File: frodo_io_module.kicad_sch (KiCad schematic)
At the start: 123 parts, among them J1 Molex MicroFit 2x3, J1 SWD, J2 Molex MicroFit 2x3, J4 JST-GH 4Pin, Q17 NMOS, Q18 NMOS, SW1 SW_DIP_x06, U1 AZ1117H-ADJ, U1 STM32F072RBT6, U3 AZ1117-3.3, U4 W25Q128JVP, U5 MCP2562-E-SN, U6 L7805, U7 L7805, U8 MCP4017-xxxxLT, U9 LM3488MM, Y1 8MHz 12pF

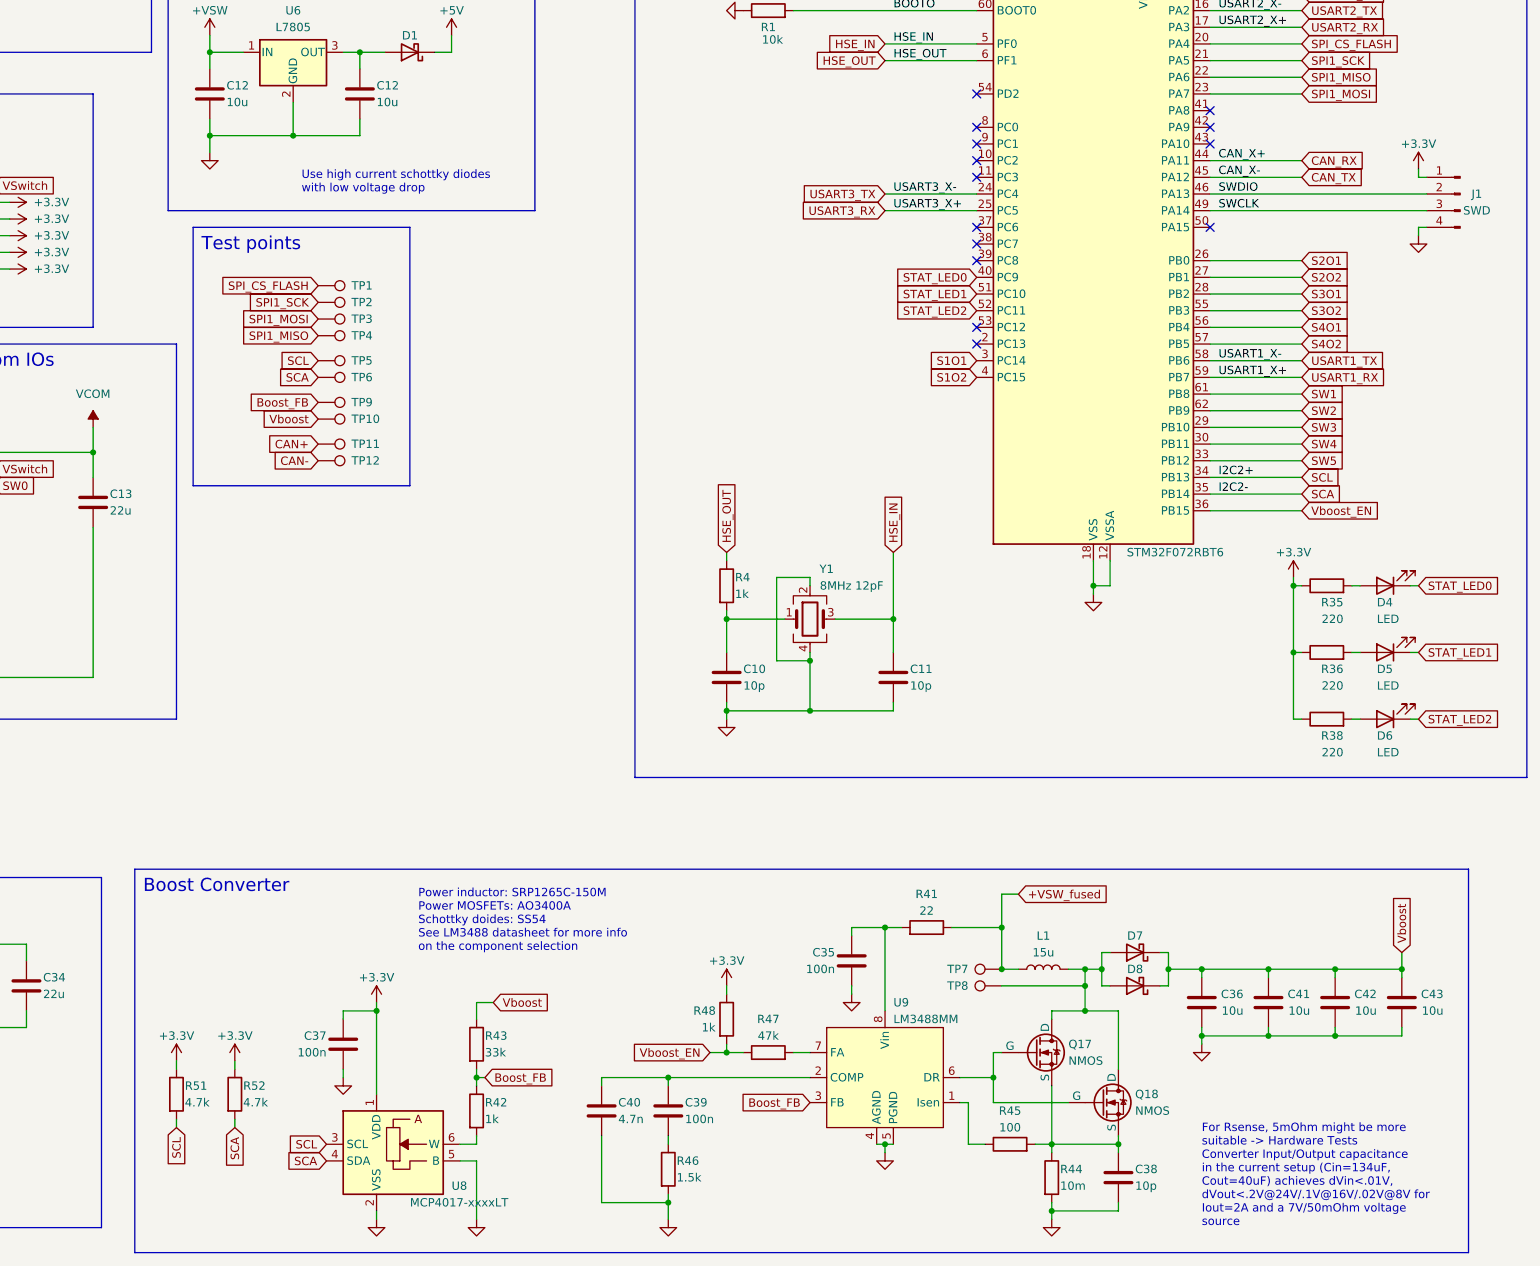
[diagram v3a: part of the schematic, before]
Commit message: Add voltage sensing, Correct resistor value
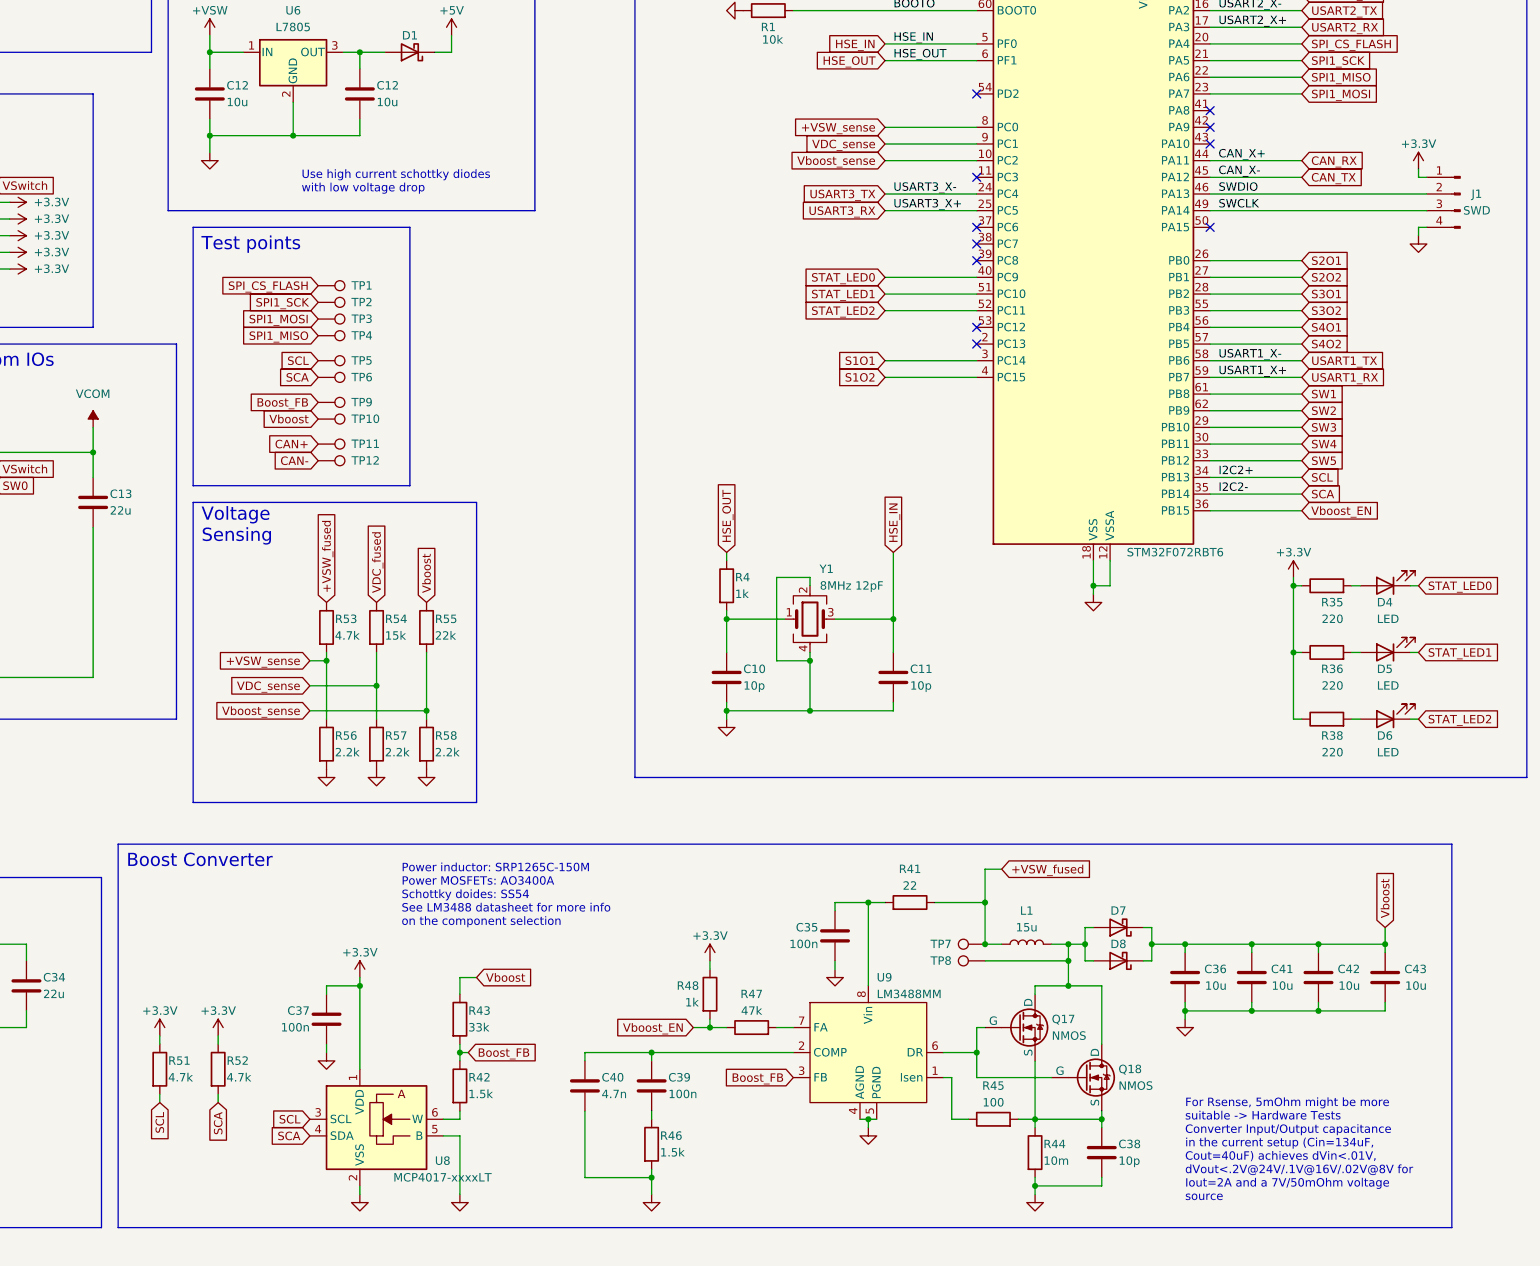
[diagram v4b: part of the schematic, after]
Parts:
- added R53: 4.7k, symbol Device:R
- added R54: 15k, symbol Device:R
- added R55: 22k, symbol Device:R
- added R56, R57, R58: 2.2k, symbol Device:R
- R42: value 1k -> 1.5k
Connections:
- net +VSW_fused: now also R53.1
- net GND: now also R56.2, R57.2, R58.2
- net VDC_fused: now also R54.1
- net Vboost: now also R55.1
- net Vboost_sense: now reaches U1.10 (PC2)
- net Vboost_sense: now also R55.2, R58.1
- net +VSW_sense: now reaches U1.8 (PC0)
- net +VSW_sense: now also R53.2, R56.1
- net VDC_sense: now reaches U1.9 (PC1)
- net VDC_sense: now also R54.2, R57.1
- no-connect marks 16 -> 13
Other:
- note added: "Voltage Sensing"
- moved on the sheet: C35, C36, C37, C38, C39, C40, C41, C42, C43, D7, D8, L1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

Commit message: footprints assigned
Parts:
- C1, C10, C11, C2, C3, C35, C37, C38, C39, C4, C9: footprint (none) -> Capacitor_SMD:C_0603_1608Metric_Pad1.08x0.95mm_HandSolder
- C12, C13, C25, C26, C27, C28, C30, C31, C32, C33, C34, C36, C41, C42, C43, C5: footprint (none) -> Capacitor_SMD:C_1206_3216Metric_Pad1.33x1.80mm_HandSolder
- C23, C24, C29, C6, C7, C8: footprint (none) -> Capacitor_SMD:C_0805_2012Metric_Pad1.18x1.45mm_HandSolder
- C43: footprint Capacitor_SMD:C_0402_1005Metric_Pad0.74x0.62mm_HandSolder -> Capacitor_SMD:C_0603_1608Metric_Pad1.08x0.95mm_HandSolder
- D3, D4, D5, D6: footprint (none) -> LED_SMD:LED_0603_1608Metric
- FB1: footprint (none) -> Ferrite_THT:LairdTech_28C0236-0JW-10
- J1, J2: footprint (none) -> Connector_Molex:Molex_Micro-Fit_3.0_43045-0600_2x03_P3.00mm_Horizontal
- J4: footprint (none) -> Connector_JST:JST_GH_SM04B-GHS-TB_1x04-1MP_P1.25mm_Horizontal
- Q17, Q18: footprint (none) -> Package_TO_SOT_SMD:SOT-23-3
- R1, R10, R4, R48, R5, R6, R7, R8, R9: footprint (none) -> Resistor_SMD:R_0603_1608Metric_Pad0.98x0.95mm_HandSolder
- R35, R36, R37, R38, R39, R40, R45: footprint (none) -> Resistor_SMD:R_0603_1608Metric
- U3: footprint (none) -> Package_TO_SOT_SMD:SOT-223-3_TabPin2
- U6, U7: footprint (none) -> Package_TO_SOT_SMD:TO-252-2
- Y1: footprint (none) -> Crystal:Crystal_SMD_5032-4Pin_5.0x3.2mm

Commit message: more footprints assigned
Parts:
- C40: footprint (none) -> Capacitor_SMD:C_1210_3225Metric_Pad1.33x2.70mm_HandSolder
- D1, D2, D7, D8: footprint (none) -> Diode_SMD:D_SOD-323_HandSoldering
- F1, F2: footprint (none) -> Fuse:Fuse_1206_3216Metric_Pad1.42x1.75mm_HandSolder
- J1, R1, R41, R42, R43, R44, R46, R49, R50, R51, R52, R53, R54, R55, R56, R57, R58: footprint (none) -> Resistor_SMD:R_0805_2012Metric_Pad1.20x1.40mm_HandSolder
- Q18: footprint Package_TO_SOT_SMD:SOT-23-3 -> Resistor_SMD:R_0805_2012Metric_Pad1.20x1.40mm_HandSolder
- R3, R47: footprint (none) -> Resistor_SMD:R_1206_3216Metric_Pad1.30x1.75mm_HandSolder
- R35, R36, R38, R39, R40, R45: footprint Resistor_SMD:R_0603_1608Metric -> Resistor_SMD:R_0603_1608Metric_Pad0.98x0.95mm_HandSolder
- R37: footprint Resistor_SMD:R_0603_1608Metric -> Resistor_SMD:R_0805_2012Metric_Pad1.20x1.40mm_HandSolder
- U9: footprint (none) -> Package_SO:TSSOP-8_4.4x3mm_P0.65mm
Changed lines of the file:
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@@
       (effects (font (size 1.27 1.27)) (justify left))
     )
-    (property "Footprint" "" (at 93.472 82.55 90)
+    (property "Footprint" "Resistor_SMD:R_0805_2012Metric_Pad1.20x1.40mm_HandSolder" (at 93.472 82.55 90)
       (effects (font (size 1.27 1.27)) hide)
     )
@@
       (effects (font (size 1.27 1.27)) (justify left))
     )
-    (property "Footprint" "" (at 195.072 213.36 90)
+    (property "Footprint" "Resistor_SMD:R_0805_2012Metric_Pad1.20x1.40mm_HandSolder" (at 195.072 213.36 90)
       (effects (font (size 1.27 1.27)) hide)
     )
@@
       (effects (font (size 1.27 1.27)) (justify left))
     )
-    (property "Footprint" "" (at 220.472 146.05 90)
+    (property "Footprint" "Resistor_SMD:R_0805_2012Metric_Pad1.20x1.40mm_HandSolder" (at 220.472 146.05 90)
       (effects (font (size 1.27 1.27)) hide)
     )
@@
       (effects (font (size 1.27 1.27)) (justify left))
     )
-    (property "Footprint" "" (at 203.962 213.36 90)
+    (property "Footprint" "Resistor_SMD:R_0805_2012Metric_Pad1.20x1.40mm_HandSolder" (at 203.962 213.36 90)
       (effects (font (size 1.27 1.27)) hide)
     )
@@
       (effects (font (size 1.27 1.27)) (justify left))
     )
-    (property "Footprint" "" (at 304.8 210.82 0)
+    (property "Footprint" "Package_SO:TSSOP-8_4.4x3mm_P0.65mm" (at 304.8 210.82 0)
       (effects (font (size 1.27 1.27)) hide)
     )
@@
       (effects (font (size 1.27 1.27)) (justify left))
     )
-    (property "Footprint" "Resistor_SMD:R_0603_1608Metric" (at 374.65 161.798 90)
+    (property "Footprint" "Resistor_SMD:R_0603_1608Metric_Pad0.98x0.95mm_HandSolder" (at 374.65 161.798 90)
       (effects (font (size 1.27 1.27)) hide)
     )
@@
       (effects (font (size 1.27 1.27)) (justify left))
     )
-    (property "Footprint" "Package_TO_SOT_SMD:SOT-23-3" (at 342.9 212.09 0)
+    (property "Footprint" "Resistor_SMD:R_0805_2012Metric_Pad1.20x1.40mm_HandSolder" (at 342.9 212.09 0)
       (effects (font (size 1.27 1.27)) hide)
     )
@@
       (effects (font (size 1.27 1.27)) (justify left))
     )
-    (property "Footprint" "" (at 168.402 129.54 90)
+    (property "Footprint" "Resistor_SMD:R_1206_3216Metric_Pad1.30x1.75mm_HandSolder" (at 168.402 129.54 90)
       (effects (font (size 1.27 1.27)) hide)
     )
@@
       (effects (font (size 1.27 1.27)))
     )
-    (property "Footprint" "" (at 394.97 80.01 0)
+    (property "Footprint" "Resistor_SMD:R_0805_2012Metric_Pad1.20x1.40mm_HandSolder" (at 394.97 80.01 0)
       (effects (font (size 1.27 1.27)) hide)
     )
@@
       (effects (font (size 1.27 1.27)) (justify left))
     )
-    (property "Footprint" "Resistor_SMD:R_0603_1608Metric" (at 374.65 151.638 90)
+    (property "Footprint" "Resistor_SMD:R_0603_1608Metric_Pad0.98x0.95mm_HandSolder" (at 374.65 151.638 90)
       (effects (font (size 1.27 1.27)) hide)
     )
@@
       (effects (font (size 1.27 1.27)))
     )
-    (property "Footprint" "" (at 287.02 208.788 90)
+    (property "Footprint" "Resistor_SMD:R_1206_3216Metric_Pad1.30x1.75mm_HandSolder" (at 287.02 208.788 90)
       (effects (font (size 1.27 1.27)) hide)
     )
@@
       (effects (font (size 1.27 1.27)) (justify left))
     )
-    (property "Footprint" "" (at 228.092 146.05 90)
+    (property "Footprint" "Resistor_SMD:R_0805_2012Metric_Pad1.20x1.40mm_HandSolder" (at 228.092 146.05 90)
       (effects (font (size 1.27 1.27)) hide)
     )
@@
       (effects (font (size 1.27 1.27)) (justify left))
     )
-    (property "Footprint" "" (at 270.002 224.79 90)
+    (property "Footprint" "Resistor_SMD:R_0805_2012Metric_Pad1.20x1.40mm_HandSolder" (at 270.002 224.79 90)
       (effects (font (size 1.27 1.27)) hide)
     )
@@
       (effects (font (size 1.27 1.27)))
     )
-    (property "Footprint" "" (at 311.15 189.738 90)
+    (property "Footprint" "Resistor_SMD:R_0805_2012Metric_Pad1.20x1.40mm_HandSolder" (at 311.15 189.738 90)
       (effects (font (size 1.27 1.27)) hide)
     )
@@
       (effects (font (size 1.27 1.27)) (justify left))
     )
-    (property "Footprint" "" (at 220.472 163.83 90)
+    (property "Footprint" "Resistor_SMD:R_0805_2012Metric_Pad1.20x1.40mm_HandSolder" (at 220.472 163.83 90)
       (effects (font (size 1.27 1.27)) hide)
     )
@@
       (effects (font (size 1.27 1.27)) (justify left))
     )
-    (property "Footprint" "Resistor_SMD:R_0603_1608Metric" (at 374.65 141.478 90)
+    (property "Footprint" "Resistor_SMD:R_0603_1608Metric_Pad0.98x0.95mm_HandSolder" (at 374.65 141.478 90)
       (effects (font (size 1.27 1.27)) hide)
     )
@@
       (effects (font (size 1.27 1.27)) (justify left))
     )
-    (property "Footprint" "" (at 235.712 146.05 90)
+    (property "Footprint" "Resistor_SMD:R_0805_2012Metric_Pad1.20x1.40mm_HandSolder" (at 235.712 146.05 90)
       (effects (font (size 1.27 1.27)) hide)
     )
@@
       (effects (font (size 1.27 1.27)) (justify left))
     )
-    (property "Footprint" "" (at 160.782 129.54 90)
+    (property "Footprint" "Resistor_SMD:R_0805_2012Metric_Pad1.20x1.40mm_HandSolder" (at 160.782 129.54 90)
       (effects (font (size 1.27 1.27)) hide)
     )
@@
       (effects (font (size 1.27 1.27)) (justify left))
     )
-    (property "Footprint" "Resistor_SMD:R_0603_1608Metric" (at 160.782 148.59 90)
+    (property "Footprint" "Resistor_SMD:R_0603_1608Metric_Pad0.98x0.95mm_HandSolder" (at 160.782 148.59 90)
       (effects (font (size 1.27 1.27)) hide)
     )
@@
       (effects (font (size 1.27 1.27)) (justify left))
     )
-    (property "Footprint" "" (at 99.06 196.088 90)
+    (property "Footprint" "Fuse:Fuse_1206_3216Metric_Pad1.42x1.75mm_HandSolder" (at 99.06 196.088 90)
       (effects (font (size 1.27 1.27)) hide)
     )
@@
       (effects (font (size 1.27 1.27)) (justify left))
     )
-    (property "Footprint" "Resistor_SMD:R_0603_1608Metric" (at 239.522 34.29 90)
+    (property "Footprint" "Resistor_SMD:R_0805_2012Metric_Pad1.20x1.40mm_HandSolder" (at 239.522 34.29 90)
       (effects (font (size 1.27 1.27)) hide)
     )
@@
       (effects (font (size 1.27 1.27)) hide)
     )
-    (property "Footprint" "" (at 342.9 191.77 0)
+    (property "Footprint" "Diode_SMD:D_SOD-323_HandSoldering" (at 342.9 191.77 0)
       (effects (font (size 1.27 1.27)) hide)
     )
@@
       (effects (font (size 1.27 1.27)) (justify left))
     )
-    (property "Footprint" "" (at 328.422 226.06 90)
+    (property "Footprint" "Resistor_SMD:R_0805_2012Metric_Pad1.20x1.40mm_HandSolder" (at 328.422 226.06 90)
       (effects (font (size 1.27 1.27)) hide)
     )
@@
       (effects (font (size 1.27 1.27)) (justify left))
     )
-    (property "Footprint" "" (at 240.792 205.74 90)
+    (property "Footprint" "Resistor_SMD:R_0805_2012Metric_Pad1.20x1.40mm_HandSolder" (at 240.792 205.74 90)
       (effects (font (size 1.27 1.27)) hide)
     )
@@
       (effects (font (size 1.27 1.27)) (justify left))
     )
-    (property "Footprint" "" (at 240.792 215.9 90)
+    (property "Footprint" "Resistor_SMD:R_0805_2012Metric_Pad1.20x1.40mm_HandSolder" (at 240.792 215.9 90)
       (effects (font (size 1.27 1.27)) hide)
     )
@@
       (effects (font (size 1.27 1.27)) (justify left))
     )
-    (property "Footprint" "" (at 262.5852 219.71 0)
+    (property "Footprint" "Capacitor_SMD:C_1210_3225Metric_Pad1.33x2.70mm_HandSolder" (at 262.5852 219.71 0)
       (effects (font (size 1.27 1.27)) hide)
     )
@@
       (effects (font (size 1.27 1.27)))
     )
-    (property "Footprint" "Resistor_SMD:R_0603_1608Metric" (at 323.85 222.758 90)
+    (property "Footprint" "Resistor_SMD:R_0603_1608Metric_Pad0.98x0.95mm_HandSolder" (at 323.85 222.758 90)
       (effects (font (size 1.27 1.27)) hide)
     )
@@
       (effects (font (size 1.27 1.27)) hide)
     )
-    (property "Footprint" "" (at 234.95 27.94 0)
+    (property "Footprint" "Diode_SMD:D_SOD-323_HandSoldering" (at 234.95 27.94 0)
       (effects (font (size 1.27 1.27)) hide)
     )
@@
       (effects (font (size 1.27 1.27)) (justify left))
     )
-    (property "Footprint" "" (at 99.06 220.218 90)
+    (property "Footprint" "Fuse:Fuse_1206_3216Metric_Pad1.42x1.75mm_HandSolder" (at 99.06 220.218 90)
       (effects (font (size 1.27 1.27)) hide)
     )
@@
       (effects (font (size 1.27 1.27)) (justify left))
     )
-    (property "Footprint" "" (at 228.092 163.83 90)
+    (property "Footprint" "Resistor_SMD:R_0805_2012Metric_Pad1.20x1.40mm_HandSolder" (at 228.092 163.83 90)
       (effects (font (size 1.27 1.27)) hide)
     )
@@
       (effects (font (size 1.27 1.27)) hide)
     )
-    (property "Footprint" "" (at 234.95 58.42 0)
+    (property "Footprint" "Diode_SMD:D_SOD-323_HandSoldering" (at 234.95 58.42 0)
       (effects (font (size 1.27 1.27)) hide)
     )
@@
       (effects (font (size 1.27 1.27)) (justify left))
     )
-    (property "Footprint" "" (at 235.712 163.83 90)
+    (property "Footprint" "Resistor_SMD:R_0805_2012Metric_Pad1.20x1.40mm_HandSolder" (at 235.712 163.83 90)
       (effects (font (size 1.27 1.27)) hide)
     )
@@
       (effects (font (size 1.27 1.27)) (justify left))
     )
-    (property "Footprint" "" (at 102.362 82.55 90)
+    (property "Footprint" "Resistor_SMD:R_0805_2012Metric_Pad1.20x1.40mm_HandSolder" (at 102.362 82.55 90)
       (effects (font (size 1.27 1.27)) hide)
     )
@@
       (effects (font (size 1.27 1.27)) hide)
     )
-    (property "Footprint" "" (at 342.9 196.85 0)
+    (property "Footprint" "Diode_SMD:D_SOD-323_HandSoldering" (at 342.9 196.85 0)
       (effects (font (size 1.27 1.27)) hide)
     )
@@
       (effects (font (size 1.27 1.27)) (justify left))
     )
-    (property "Footprint" "Resistor_SMD:R_0603_1608Metric" (at 115.57 44.45 0)
+    (property "Footprint" "Resistor_SMD:R_0603_1608Metric_Pad0.98x0.95mm_HandSolder" (at 115.57 44.45 0)
       (effects (font (size 1.27 1.27)) hide)
     )

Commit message: Finish footprint assignment
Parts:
- C40: value 4.7n -> 3.3n; footprint Capacitor_SMD:C_1210_3225Metric_Pad1.33x2.70mm_HandSolder -> Capacitor_SMD:C_0603_1608Metric_Pad1.08x0.95mm_HandSolder
- C6: value 10n -> 22n; footprint Capacitor_SMD:C_0805_2012Metric_Pad1.18x1.45mm_HandSolder -> Capacitor_SMD:C_0603_1608Metric_Pad1.08x0.95mm_HandSolder
- D1, D2, D7, D8: footprint Diode_SMD:D_SOD-323_HandSoldering -> Diode_SMD:D_SOD-123F
- FB1: footprint Ferrite_THT:LairdTech_28C0236-0JW-10 -> Inductor_SMD:L_0603_1608Metric_Pad1.05x0.95mm_HandSolder
- J1: footprint Resistor_SMD:R_0805_2012Metric_Pad1.20x1.40mm_HandSolder -> Connector_PinHeader_2.54mm:PinHeader_1x04_P2.54mm_Vertical
- JP1, JP2, JP3, JP4, JP5, JP6, JP7, JP8: footprint (none) -> Jumper:SolderJumper-2_P1.3mm_Open_RoundedPad1.0x1.5mm
- L1: footprint (none) -> Inductor_SMD:L_Bourns_SRP1245A
- Q17: footprint Package_TO_SOT_SMD:SOT-23-3 -> Package_TO_SOT_SMD:SOT-23
- Q18: footprint Resistor_SMD:R_0805_2012Metric_Pad1.20x1.40mm_HandSolder -> Package_TO_SOT_SMD:SOT-23
- R1, R37, R41, R42, R43, R46, R49, R50, R51, R52, R53, R54, R55, R56, R57, R58: footprint Resistor_SMD:R_0805_2012Metric_Pad1.20x1.40mm_HandSolder -> Resistor_SMD:R_0603_1608Metric_Pad0.98x0.95mm_HandSolder
- R3, R47: footprint Resistor_SMD:R_1206_3216Metric_Pad1.30x1.75mm_HandSolder -> Resistor_SMD:R_0603_1608Metric_Pad0.98x0.95mm_HandSolder
- R44: footprint Resistor_SMD:R_0805_2012Metric_Pad1.20x1.40mm_HandSolder -> Resistor_SMD:R_2512_6332Metric_Pad1.40x3.35mm_HandSolder
- R48: value 1k -> 1.5k
- R9: value 1OK -> 10K
- SW1: footprint (none) -> Button_Switch_SMD:SW_DIP_SPSTx06_Slide_9.78x17.42mm_W8.61mm_P2.54mm
- TP1, TP10, TP11, TP12, TP2, TP3, TP4, TP5, TP6, TP7, TP8, TP9: footprint (none) -> TestPoint:TestPoint_Pad_2.0x2.0mm
- U9: footprint Package_SO:TSSOP-8_4.4x3mm_P0.65mm -> Package_SO:MSOP-8_3x3mm_P0.65mm
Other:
- note added: "C11 should be 10nF, but 22nF is easier available"
- note added: "C40 should be 4.7nF, but 3.3nF is easier available"
